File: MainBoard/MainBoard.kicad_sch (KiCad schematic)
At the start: 45 parts, among them J1 1761681-3, Q1 BC557, U1 TL074

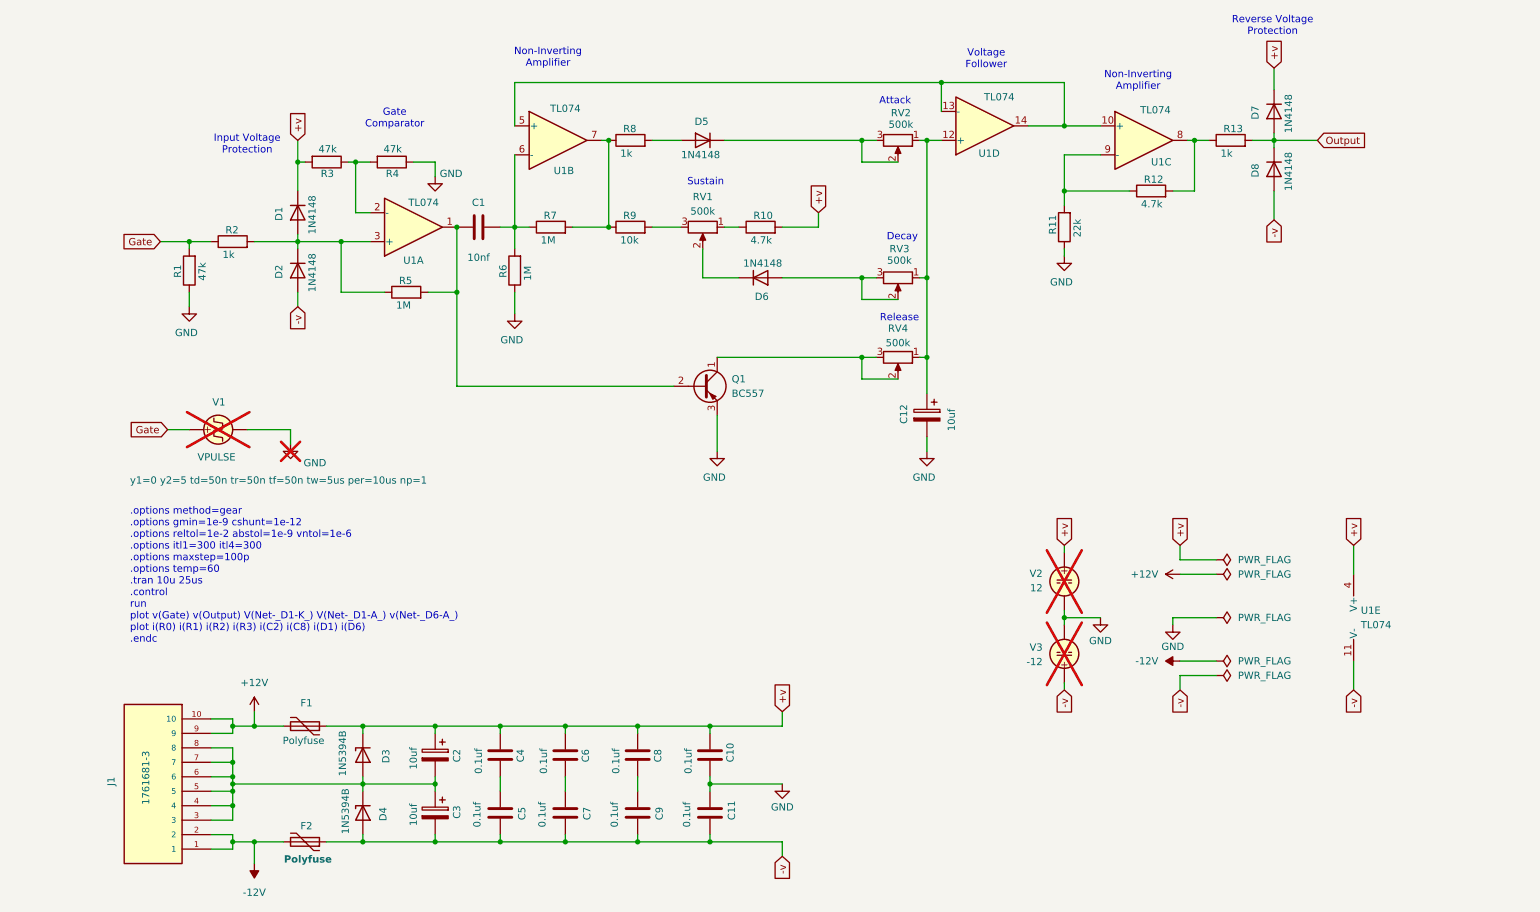
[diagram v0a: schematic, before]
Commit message: functional comparator stage
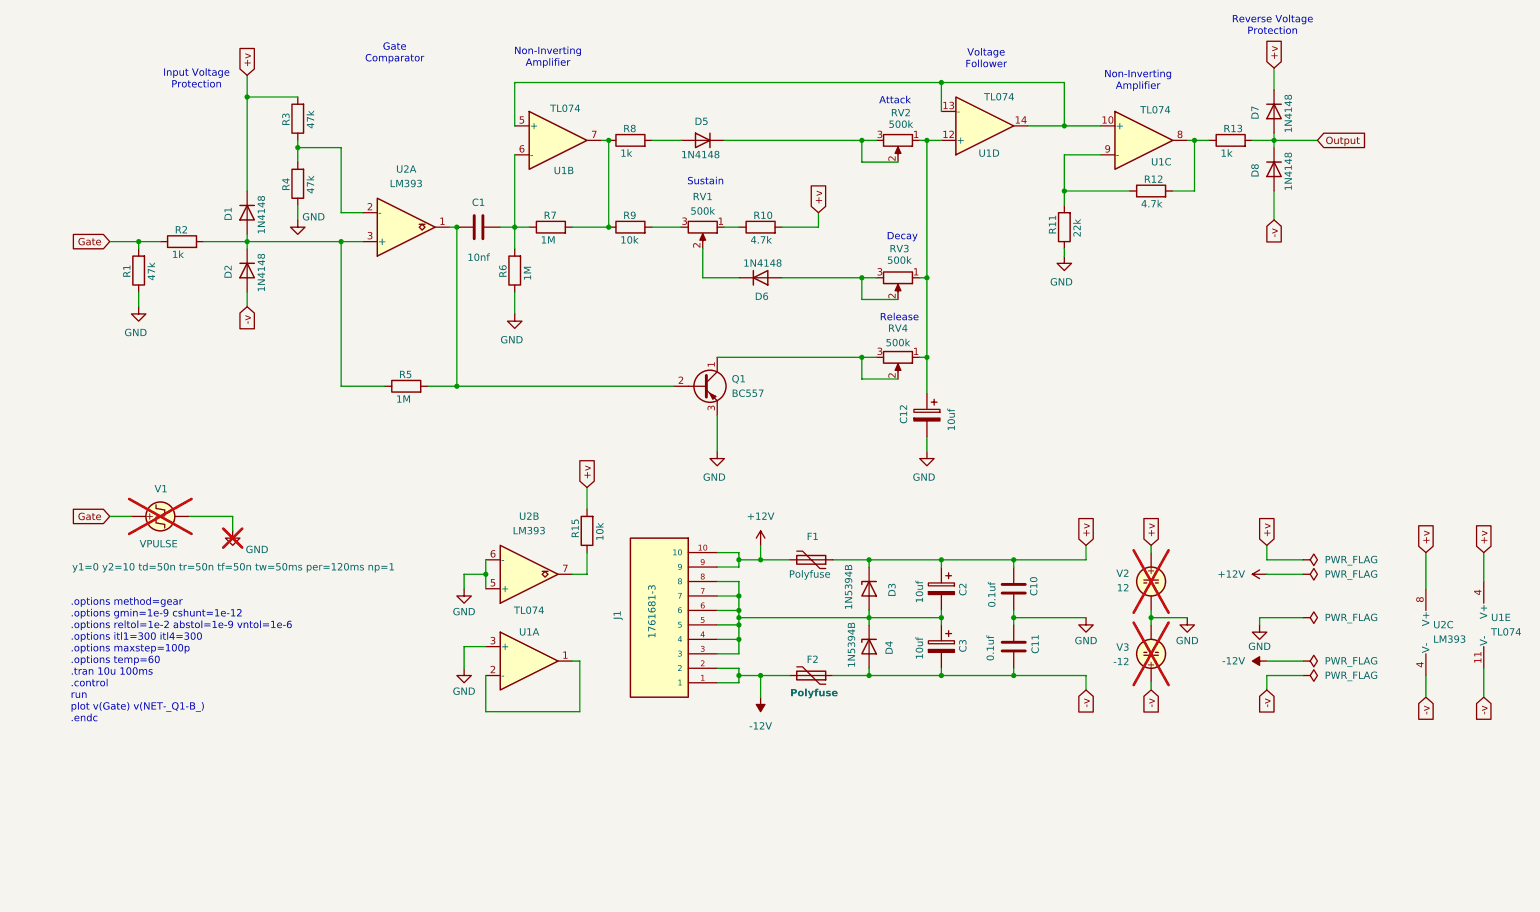
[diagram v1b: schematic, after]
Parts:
- removed C4, C5, C6, C7, C8, C9: 0.1uf, symbol Device:C
- added R15: 10k, symbol Device:R
- added U2: LM393, symbol Comparator:LM393
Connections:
- net +v: now also R15.2, U2.8 (V+)
- net -v: now also U2.4 (V-)
- net GND: now also U1.3 (+), U2.5 (+), U2.6 (-)
- net at D1.2 (A), D2.1 (K), R2.2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: now also U2.3 (+); no longer U1.3 (+)
- net at R3.1, R4.2: now also U2.2 (-); no longer U1.2 (-)
- net at C1.1, Q1.2 (B), R5.2: now also U2.1; no longer U1.1
- new net: U1.1, U1.2 (-)
- new net: R15.1, U2.7
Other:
- note added: ".options method=gear .options gmin=1e-9 cshunt=1e-12 .options reltol=1e-2 abstol=1e-9 vntol=1e-6 .options itl1=300 itl4=300 .options maxstep=100p .options temp=60 .tran 10u 100ms .control run plot v(Gate) v(NET-_Q1-B_) .endc"
- note removed: ".options method=gear .options gmin=1e-9 cshunt=1e-12 .options reltol=1e-2 abstol=1e-9 vntol=1e-6 .options itl1=300 itl4=300 .options maxstep=100p .options temp=60 .tran 10u 25us .control run plot v(Gate) v(Output) V(Net-_D1-K_) V(Net-_D1-A_) v(Net-_D6-A_) plot i(R0) i(R1) i(R2) i(R3) i(C2) i(C8) i(D1) i(D6) .endc"
- moved on the sheet: C10, C11, C2, C3, D1, D2, D3, D4, F1, F2, J1, R1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

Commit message: WIP: still need to figure out why kicad is flipping the power pins on the TL047 when exporting the netlist.  the comparator may also need a pullup resistor
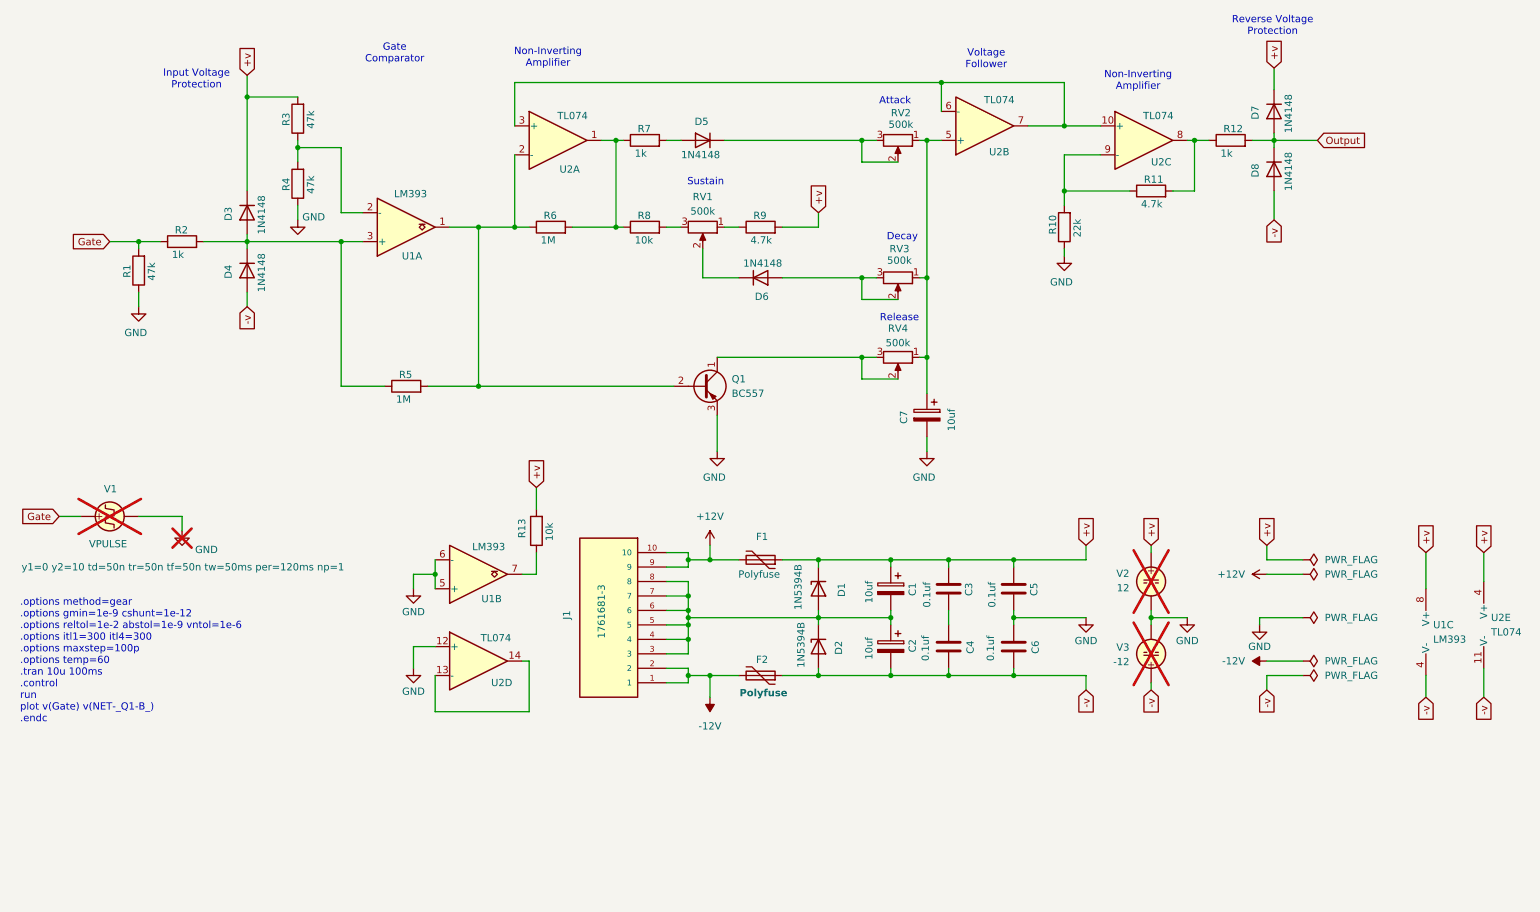
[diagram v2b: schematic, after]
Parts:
- removed C1: 10nf, symbol Device:C
- removed R6: 1M, symbol Device:R
- added C3, C4: 0.1uf, symbol Device:C
- renumbered C2 to C1, C3 to C2, C10 to C5, C11 to C6, C12 to C7, D3 to D1, D4 to D2, D1 to D3, D2 to D4, R11 to R10, R12 to R11, R13 to R12, R15 to R13, R7 to R6, R8 to R7, R9 to R8, R10 to R9, U2 to U1, U1 to U2
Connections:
- net +v: now also C3.1
- net -v: now also C4.2
- net GND: now also U2.12 (+); no longer U2.3 (+)
- net at C7.1, RV2.1, RV3.1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: now also U2.5 (+); no longer U2.12 (+)
- net at R6.2, R7.1, R8.1: now also U2.1; no longer U2.7
- net at R6.1: now also Q1.2 (B), R5.2, U1.1, U2.2 (-); no longer U2.6 (-)
- new net: C3.2, C4.1
- new net: U2.10 (+), U2.3 (+), U2.6 (-), U2.7
- new net: U2.13 (-), U2.14
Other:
- moved on the sheet: C1, C2, D1, D2, F1, F2, J1, R13, R7, R8, U1B, U2D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

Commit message: added pull-up resistor and updated lm393 model
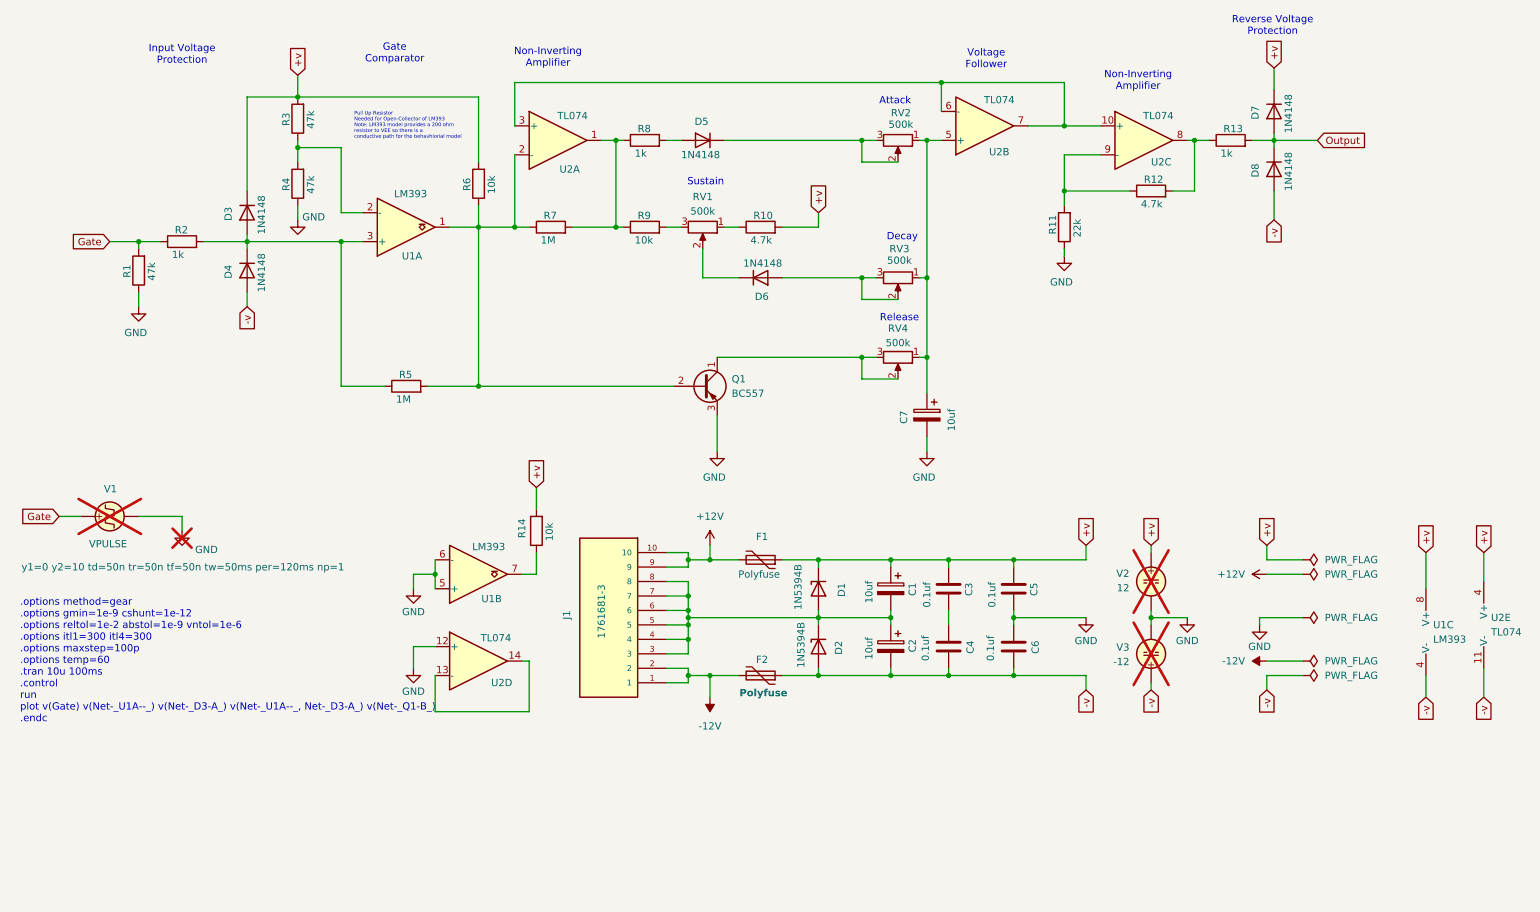
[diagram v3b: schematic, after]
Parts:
- added R6: 10k, symbol Device:R
- renumbered R9 to R10, R10 to R11, R11 to R12, R12 to R13, R13 to R14, R6 to R7, R7 to R8, R8 to R9
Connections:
- net +v: now also R6.2
- net at Q1.2 (B), R5.2, R7.1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: now also R6.1
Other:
- note added: ".options method=gear .options gmin=1e-9 cshunt=1e-12 .options reltol=1e-2 abstol=1e-9 vntol=1e-6 .options itl1=300 itl4=300 .options maxstep=100p .options temp=60 .tran 10u 100ms .control run plot v(Gate) v(Net-_U1A--_) v(Net-_D3-A_) v(Net-_U1A--_, Net-_D3-A_) v(Net-_Q1-B_) .endc"
- note added: "Pull Up Resistor Needed for Open-Collector of LM393 Note: LM393 model provides a 200 ohm resistor to VEE so there is a conductive path for the behavhiorial model"
- note removed: ".options method=gear .options gmin=1e-9 cshunt=1e-12 .options reltol=1e-2 abstol=1e-9 vntol=1e-6 .options itl1=300 itl4=300 .options maxstep=100p .options temp=60 .tran 10u 100ms .control run plot v(Gate) v(NET-_Q1-B_) .endc"
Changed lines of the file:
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@@
 		)
 	)
+	(text "Pull Up Resistor\nNeeded for Open-Collector of LM393\nNote: LM393 model provides a 200 ohm\nresistor to VEE so there is a \nconductive path for the behavhiorial model"
+		(exclude_from_sim no)
+		(at 75.946 55.88 0)
+		(effects
+			(font
+				(size 0.635 0.635)
+			)
+			(justify left)
+		)
+	)
 	(text "Gate \nComparator"
 		(exclude_from_sim no)
@@
 	(text "Input Voltage\nProtection"
 		(exclude_from_sim no)
-		(at 48.26 47.752 0)
+		(at 45.72 43.434 0)
 		(effects
 			(font
@@
 		)
 	)
-	(text ".options method=gear \n.options gmin=1e-9 cshunt=1e-12 \n.options reltol=1e-2 abstol=1e-9 vntol=1e-6 \n.options itl1=300 itl4=300 \n.options maxstep=100p\n.options temp=60\n.tran 10u 100ms\n.control\nrun\nplot v(Gate) v(NET-_Q1-B_)\n.endc\n"
+	(text ".options method=gear \n.options gmin=1e-9 cshunt=1e-12 \n.options reltol=1e-2 abstol=1e-9 vntol=1e-6 \n.options itl1=300 itl4=300 \n.options maxstep=100p\n.options temp=60\n.tran 10u 100ms\n.control\nrun\nplot v(Gate) v(Net-_U1A--_) v(Net-_D3-A_) v(Net-_U1A--_, Net-_D3-A_) v(Net-_Q1-B_)\n.endc\n"
 		(exclude_from_sim no)
 		(at 17.272 149.86 0)
@@
 	)
 	(junction
-		(at 57.15 50.8)
-		(diameter 0)
-		(color 0 0 0 0)
-	)
-	(junction
 		(at 66.04 59.69)
 		(diameter 0)
@@
 	)
 	(junction
+		(at 66.04 50.8)
+		(diameter 0)
+		(color 0 0 0 0)
+	)
+	(junction
 		(at 176.53 58.42)
 		(diameter 0)
@@
 	(wire
 		(pts
+			(xy 66.04 50.8) (xy 97.79 50.8)
+		)
+		(stroke
+			(width 0)
+			(type default)
+		)
+	)
+	(wire
+		(pts
 			(xy 138.43 129.54) (xy 138.43 132.08)
 		)
@@
 	(wire
 		(pts
-			(xy 57.15 46.99) (xy 57.15 50.8)
+			(xy 66.04 46.99) (xy 66.04 50.8)
 		)
 		(stroke
@@
 	(wire
 		(pts
+			(xy 97.79 69.85) (xy 97.79 73.66)
+		)
+		(stroke
+			(width 0)
+			(type default)
+		)
+	)
+	(wire
+		(pts
 			(xy 138.43 152.4) (xy 134.62 152.4)
 		)
@@
 	(wire
 		(pts
+			(xy 97.79 50.8) (xy 97.79 62.23)
+		)
+		(stroke
+			(width 0)
+			(type default)
+		)
+	)
+	(wire
+		(pts
 			(xy 165.1 86.36) (xy 171.45 86.36)
 		)
@@
 	(global_label "+v"
 		(shape input)
-		(at 57.15 46.99 90)
+		(at 66.04 46.99 90)
 		(fields_autoplaced yes)
 		(effects
@@
 		)
 		(property "Intersheetrefs" "${INTERSHEET_REFS}"
-			(at 57.15 41.4648 90)
+			(at 66.04 41.4648 90)
 			(effects
 				(font
@@
 		(on_board yes)
 		(dnp no)
-		(property "Reference" "R8"
+		(property "Reference" "R9"
 			(at 125.73 71.628 90)
 			(effects
@@
 			(project "MainBoard"
 				(path "/b7fe592a-70f1-4018-a1e6-02a0fad66ba8"
-					(reference "R8")
+					(reference "R9")
 					(unit 1)
 				)
@@
 		(on_board yes)
 		(dnp no)
-		(property "Reference" "R6"
+		(property "Reference" "R7"
 			(at 109.22 71.628 90)
 			(effects
@@
 			(project "MainBoard"
 				(path "/b7fe592a-70f1-4018-a1e6-02a0fad66ba8"
-					(reference "R6")
+					(reference "R7")
 					(unit 1)
 				)
@@
 	)
 	(symbol
+		(lib_id "Device:R")
+		(at 97.79 66.04 180)
+		(unit 1)
+		(exclude_from_sim no)
+		(in_bom yes)
+		(on_board yes)
+		(dnp no)
+		(property "Reference" "R6"
+			(at 95.758 67.31 90)
+			(effects
+				(font
+					(size 1.27 1.27)
+				)
+				(justify right)
+			)
+		)
+		(property "Value" "10k"
+			(at 100.076 67.818 90)
+			(effects
+				(font
+					(size 1.27 1.27)
+				)
+				(justify right)
+			)
+		)
+		(property "Footprint" ""
+			(at 99.568 66.04 90)
+			(effects
+				(font
+					(size 1.27 1.27)
+				)
+				(hide yes)
+			)
+		)
+		(property "Datasheet" "~"
+			(at 97.79 66.04 0)
+			(effects
+				(font
+					(size 1.27 1.27)
+				)
+				(hide yes)
+			)
+		)
+		(property "Description" "Resistor"
+			(at 97.79 66.04 0)
+			(effects
+				(font
+					(size 1.27 1.27)
+				)
+				(hide yes)
+			)
+		)
+		(pin "2"
+		)
+		(pin "1"
+		)
+		(instances
+			(project "MainBoard"
+				(path "/b7fe592a-70f1-4018-a1e6-02a0fad66ba8"
+					(reference "R6")
+					(unit 1)
+				)
+			)
+		)
+	)
+	(symbol
 		(lib_id "Device:C")
 		(at 191.77 137.16 0)
@@
 		(on_board yes)
 		(dnp no)
-		(property "Reference" "R12"
+		(property "Reference" "R13"
 			(at 228.6 56.388 90)
 			(effects
@@
 			(project "MainBoard"
 				(path "/b7fe592a-70f1-4018-a1e6-02a0fad66ba8"
-					(reference "R12")
+					(reference "R13")
 					(unit 1)
 				)
@@
 		(on_board yes)
 		(dnp no)
-		(property "Reference" "R7"
+		(property "Reference" "R8"
 			(at 125.73 56.388 90)
 			(effects
@@
 			(project "MainBoard"
 				(path "/b7fe592a-70f1-4018-a1e6-02a0fad66ba8"
-					(reference "R7")
+					(reference "R8")
 					(unit 1)
 				)
@@
 		(on_board yes)
 		(dnp no)
-		(property "Reference" "R11"
+		(property "Reference" "R12"
 			(at 214.63 65.278 90)
 			(effects
@@
 			(project "MainBoard"
 				(path "/b7fe592a-70f1-4018-a1e6-02a0fad66ba8"
-					(reference "R11")
+					(reference "R12")
 					(unit 1)
 				)
@@
 		(on_board yes)
 		(dnp no)
-		(property "Reference" "R13"
+		(property "Reference" "R14"
 			(at 105.41 128.27 90)
 			(effects
@@
 			(project "MainBoard"
 				(path "/b7fe592a-70f1-4018-a1e6-02a0fad66ba8"
-					(reference "R13")
+					(reference "R14")
 					(unit 1)
 				)
@@
 		(on_board yes)
 		(dnp no)
-		(property "Reference" "R10"
+		(property "Reference" "R11"
 			(at 198.628 74.93 90)
 			(effects
@@
 			(project "MainBoard"
 				(path "/b7fe592a-70f1-4018-a1e6-02a0fad66ba8"
-					(reference "R10")
+					(reference "R11")
 					(unit 1)
 				)
@@
 		(on_board yes)
 		(dnp no)
-		(property "Reference" "R9"
+		(property "Reference" "R10"
 			(at 146.05 71.628 90)
 			(effects
@@
 			(project "MainBoard"
 				(path "/b7fe592a-70f1-4018-a1e6-02a0fad66ba8"
-					(reference "R9")
+					(reference "R10")
 					(unit 1)
 				)
